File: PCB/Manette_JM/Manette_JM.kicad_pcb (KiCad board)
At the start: 4 copper layers, 100 x 80 mm, 47 parts, among them J1 Jack 1, J10 Jack 10, J11 Jack 11, J12 Jack 12, J13 Jack 13, J14 Jack 14, J15 Bouton 1, J16 Bouton 2, J17 Bouton 3, J18 Bouton 4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

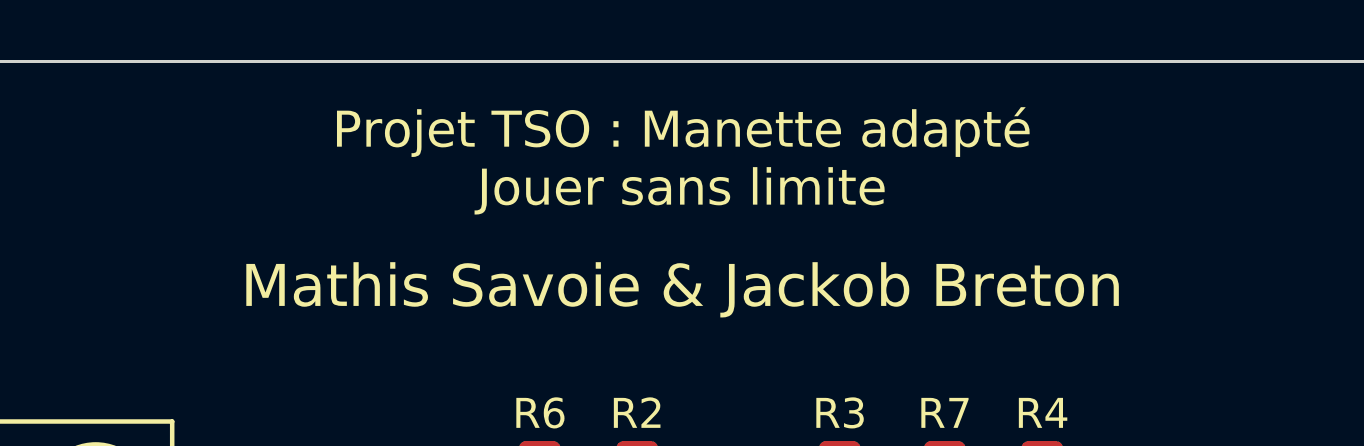
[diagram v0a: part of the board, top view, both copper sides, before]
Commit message: Quick PCB change
corrigé une faute d'orthographe
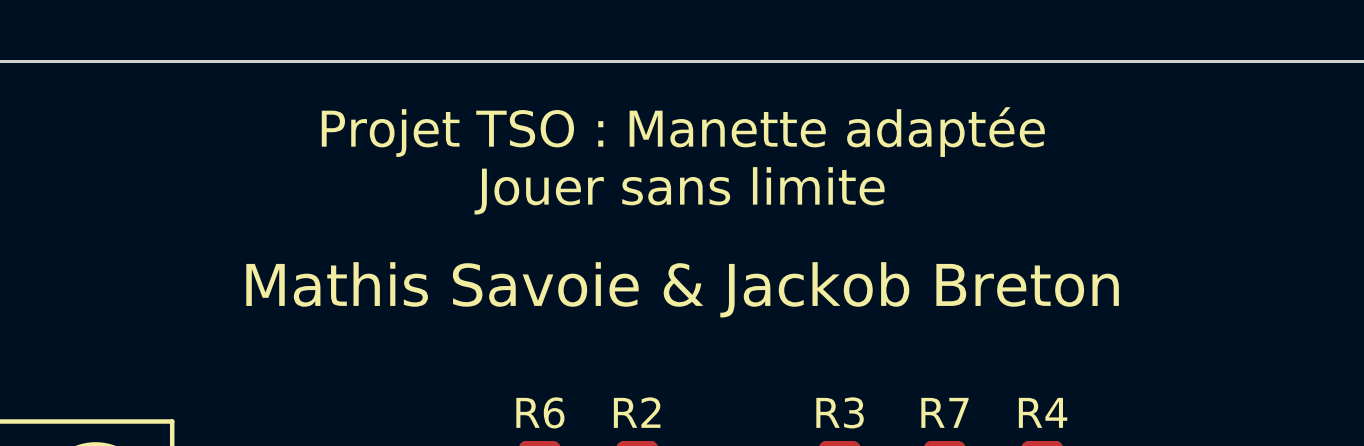
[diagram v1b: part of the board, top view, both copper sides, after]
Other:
- board text added: "Projet TSO : Manette adaptée Jouer sans limite"
- board text removed: "Projet TSO : Manette adapté Jouer sans limite"
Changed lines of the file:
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@@
   (gr_line (start 101.5 115.5) (end 201.5 115.5) (layer "Edge.Cuts") (width 0.1))
   (gr_line (start 101.5 35.5) (end 101.5 115.5) (layer "Edge.Cuts") (width 0.1))
-  (gr_text "Projet TSO : Manette adapté\nJouer sans limite\n" (at 151.5 38.75) (layer "F.SilkS")
+  (gr_text "Projet TSO : Manette adaptée\nJouer sans limite\n" (at 151.5 38.75) (layer "F.SilkS")
     (effects (font (size 1.2 1.2) (thickness 0.15)))
   )
